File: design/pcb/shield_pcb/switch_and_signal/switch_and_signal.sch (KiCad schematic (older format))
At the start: 8 parts

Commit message: May include some of the refactoring of the schematic into Arduino shield template. Updated library references b/c 2337b83b kicad build wanted it. Broke some things and will need to fix.
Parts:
- Q?: symbol IRL620 -> choice_shield:IRL620
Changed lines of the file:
@@
-EESchema Schematic File Version 3
-LIBS:choice_shield
-LIBS:power
-LIBS:device
-LIBS:linear
-LIBS:regul
-LIBS:adc-dac
-LIBS:memory
-LIBS:xilinx
-LIBS:microcontrollers
-LIBS:dsp
-LIBS:microchip
-LIBS:analog_switches
-LIBS:motorola
-LIBS:texas
-LIBS:intel
-LIBS:audio
-LIBS:interface
-LIBS:digital-audio
-LIBS:philips
-LIBS:cypress
-LIBS:siliconi
-LIBS:opto
-LIBS:atmel
-LIBS:contrib
-LIBS:Connector
-LIBS:Valve
-LIBS:Diode
-LIBS:Display
-LIBS:Transistor
-LIBS:Logic_CMOS_4000
-LIBS:Logic_74xx
+EESchema Schematic File Version 4
 LIBS:shield_pcb-cache
 EELAYER 26 0
@@
 $Descr A4 11693 8268
 encoding utf-8
-Sheet 1 1
+Sheet 10 18
 Title ""
 Date ""
@@
 AR Path="/5A04F7C4/5A020264" Ref="R?"  Part="1"
 AR Path="/5A04FF59/5A020264" Ref="R?"  Part="1"
+AR Path="/5A053B90/5A020264" Ref="R?"  Part="1"
 F 0 "R?" V 2350 2750 50  0000 L CNN
 F 1 "150" V 2450 2750 50  0000 L CNN
@@
 AR Path="/5A04F7C4/5A0202C8" Ref="R?"  Part="1"
 AR Path="/5A04FF59/5A0202C8" Ref="R?"  Part="1"
+AR Path="/5A053B90/5A0202C8" Ref="R?"  Part="1"
 F 0 "R?" H 3120 3246 50  0000 L CNN
 F 1 "100K" H 3120 3155 50  0000 L CNN
@@
 AR Path="/5A04F7C4/5A020329" Ref="R?"  Part="1"
 AR Path="/5A04FF59/5A020329" Ref="R?"  Part="1"
+AR Path="/5A053B90/5A020329" Ref="R?"  Part="1"
 F 0 "R?" H 3720 1996 50  0000 L CNN
 F 1 "150K" H 3720 1905 50  0000 L CNN
@@
 AR Path="/5A04F7C4/5A020365" Ref="R?"  Part="1"
 AR Path="/5A04FF59/5A020365" Ref="R?"  Part="1"
+AR Path="/5A053B90/5A020365" Ref="R?"  Part="1"
 F 0 "R?" V 3950 1500 50  0000 L CNN
 F 1 "160K,0.25W" V 4050 1500 50  0000 L CNN
@@
 AR Path="/5A04F7C4/5A0203AA" Ref="R?"  Part="1"
 AR Path="/5A04FF59/5A0203AA" Ref="R?"  Part="1"
+AR Path="/5A053B90/5A0203AA" Ref="R?"  Part="1"
 F 0 "R?" V 3950 2150 50  0000 L CNN
 F 1 "160K,0.25W" V 4050 2150 50  0000 L CNN
@@
 AR Path="/5A04F7C4/5A020460" Ref="D?"  Part="1"
 AR Path="/5A04FF59/5A020460" Ref="D?"  Part="1"
+AR Path="/5A053B90/5A020460" Ref="D?"  Part="1"
 F 0 "D?" V 4600 1600 50  0000 C CNN
 F 1 "D" V 4700 1550 50  0000 C CNN
@@
 AR Path="/5A04F7C4/5A020509" Ref="D?"  Part="1"
 AR Path="/5A04FF59/5A020509" Ref="D?"  Part="1"
+AR Path="/5A053B90/5A020509" Ref="D?"  Part="1"
 F 0 "D?" V 4600 2250 50  0000 C CNN
 F 1 "D" V 4700 2200 50  0000 C CNN
@@
 $EndComp
 $Comp
-L IRL620 Q?
+L choice_shield:IRL620 Q?
 U 1 1 5A04EA8A
 P 3550 2850
 AR Path="/5A04F7C4/5A04EA8A" Ref="Q?"  Part="1"
 AR Path="/5A04FF59/5A04EA8A" Ref="Q?"  Part="1"
+AR Path="/5A053B90/5A04EA8A" Ref="Q?"  Part="1"
 F 0 "Q?" H 3756 2896 50  0000 L CNN
 F 1 "IRL620" H 3756 2805 50  0000 L CNN
@@
 AR Path="/5A04F7C4/5A04F122" Ref="#PWR?"  Part="1"
 AR Path="/5A04FF59/5A04F122" Ref="#PWR?"  Part="1"
+AR Path="/5A053B90/5A04F122" Ref="#PWR?"  Part="1"
 F 0 "#PWR?" H 3350 3400 50  0001 C CNN
 F 1 "GND" H 3355 3477 50  0000 C CNN
@@
 AR Path="/5A04F7C4/5A04FCD5" Ref="#PWR?"  Part="1"
 AR Path="/5A04FF59/5A04FCD5" Ref="#PWR?"  Part="1"
+AR Path="/5A053B90/5A04FCD5" Ref="#PWR?"  Part="1"
 F 0 "#PWR?" H 4650 1750 50  0001 C CNN
 F 1 "VCC" H 4667 2073 50  0000 C CNN
@@
 AR Path="/5A04F7C4/5A04FD15" Ref="#PWR?"  Part="1"
 AR Path="/5A04FF59/5A04FD15" Ref="#PWR?"  Part="1"
+AR Path="/5A053B90/5A04FD15" Ref="#PWR?"  Part="1"
 F 0 "#PWR?" H 4650 1100 50  0001 C CNN
 F 1 "VCC" H 4667 1423 50  0000 C CNN

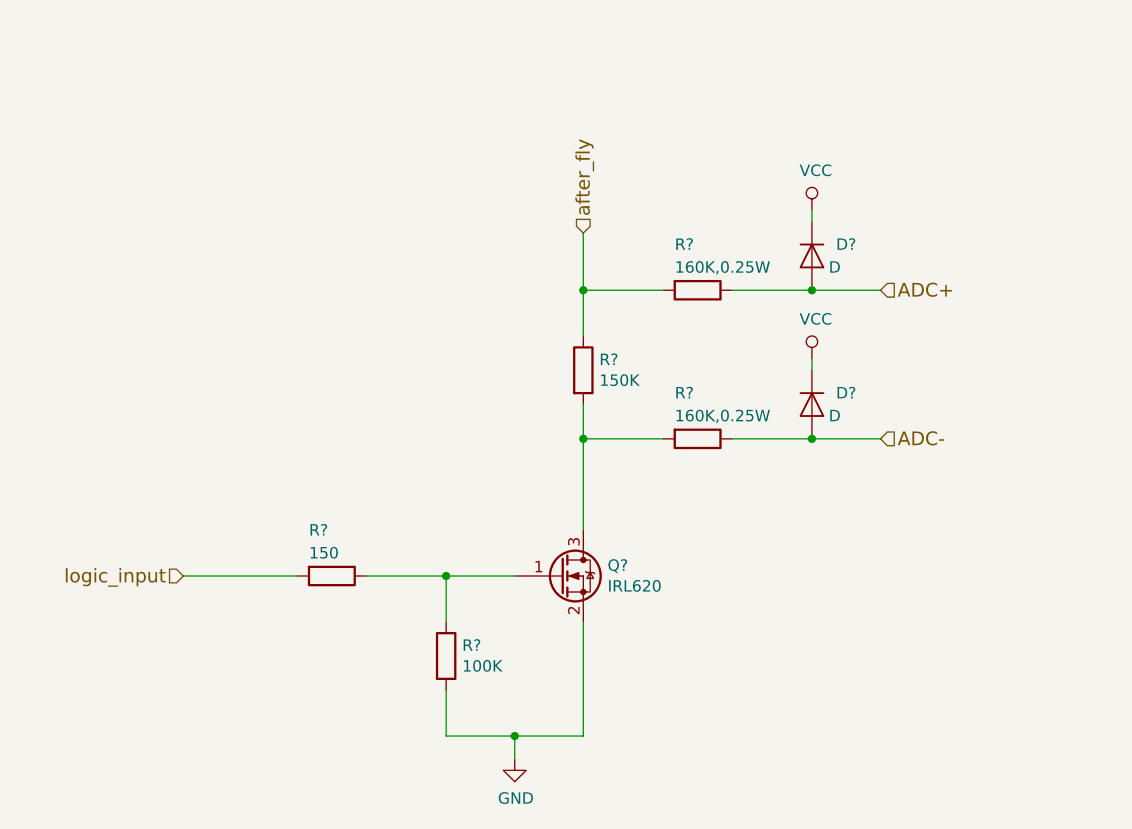
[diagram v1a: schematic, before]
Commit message: Fixed shield schematic, at least for KiCad <= d8f4e35. Added notes to single measurement unit. Updated IRL620 library part to include correct datasheet, etc.
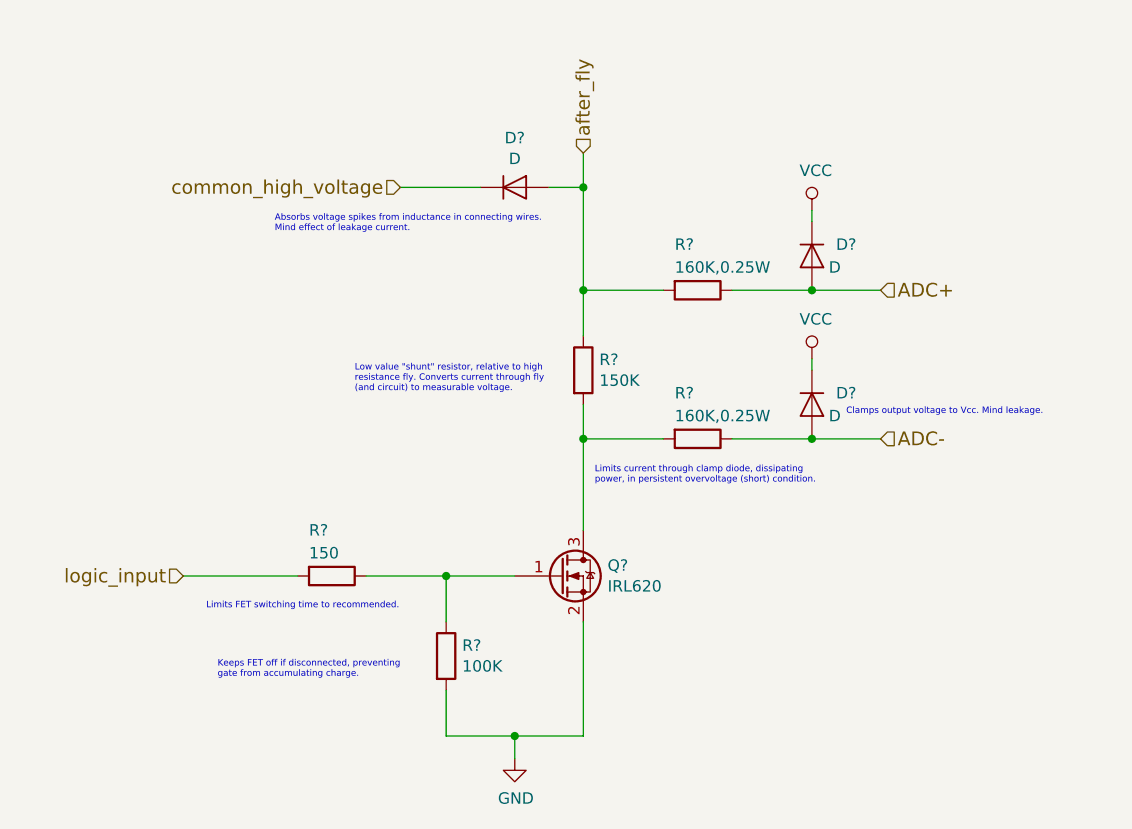
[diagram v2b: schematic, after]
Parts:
- removed Q?: IRL620, TO_SOT_Packages_THT:TO-220-3_Vertical, symbol choice_shield:IRL620
- added D?: D, symbol D
- added Q?: IRL620, TO_SOT_Packages_THT:TO-220-3_Vertical, symbol IRL620
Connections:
- net GND: now also Q?.2 (S)
- net after_fly: now also D?.2 (A)
- net at R?.1, R?.1: now also Q?.1 (G)
- net at R?.2, R?.2: now also Q?.3 (D)
- new net common_high_voltage: D?.1 (K)
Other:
- note added: "Absorbs voltage spikes from inductance in connecting wires.\nMind effect of leakage current."
- note added: "Clamps output voltage to Vcc. Mind leakage."
- note added: "Keeps FET off if disconnected, preventing \ngate from accumulating charge."
- note added: "Limits FET switching time to recommended."
- note added: "Limits current through clamp diode, dissipating \npower, in persistent overvoltage (short) condition."
- note added: "Low value "shunt" resistor, relative to high \nresistance fly. Converts current through fly \n(and circuit) to measurable voltage."
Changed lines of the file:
@@
-EESchema Schematic File Version 4
+EESchema Schematic File Version 3
+LIBS:choice_shield
+LIBS:device
+LIBS:Connector
+LIBS:Transistor
+LIBS:analog_devices
+LIBS:analog_switches
+LIBS:atmel
+LIBS:power
 LIBS:shield_pcb-cache
 EELAYER 26 0
@@
 AR Path="/5A04FF59/5A020264" Ref="R?"  Part="1"
 AR Path="/5A053B90/5A020264" Ref="R?"  Part="1"
+AR Path="/5A050A02/5A020264" Ref="R?"  Part="1"
 F 0 "R?" V 2350 2750 50  0000 L CNN
 F 1 "150" V 2450 2750 50  0000 L CNN
@@
 AR Path="/5A04FF59/5A0202C8" Ref="R?"  Part="1"
 AR Path="/5A053B90/5A0202C8" Ref="R?"  Part="1"
+AR Path="/5A050A02/5A0202C8" Ref="R?"  Part="1"
 F 0 "R?" H 3120 3246 50  0000 L CNN
 F 1 "100K" H 3120 3155 50  0000 L CNN
@@
 AR Path="/5A04FF59/5A020329" Ref="R?"  Part="1"
 AR Path="/5A053B90/5A020329" Ref="R?"  Part="1"
+AR Path="/5A050A02/5A020329" Ref="R?"  Part="1"
 F 0 "R?" H 3720 1996 50  0000 L CNN
 F 1 "150K" H 3720 1905 50  0000 L CNN
@@
 AR Path="/5A04FF59/5A020365" Ref="R?"  Part="1"
 AR Path="/5A053B90/5A020365" Ref="R?"  Part="1"
+AR Path="/5A050A02/5A020365" Ref="R?"  Part="1"
 F 0 "R?" V 3950 1500 50  0000 L CNN
 F 1 "160K,0.25W" V 4050 1500 50  0000 L CNN
@@
 AR Path="/5A04FF59/5A0203AA" Ref="R?"  Part="1"
 AR Path="/5A053B90/5A0203AA" Ref="R?"  Part="1"
+AR Path="/5A050A02/5A0203AA" Ref="R?"  Part="1"
 F 0 "R?" V 3950 2150 50  0000 L CNN
 F 1 "160K,0.25W" V 4050 2150 50  0000 L CNN
@@
 AR Path="/5A04FF59/5A020460" Ref="D?"  Part="1"
 AR Path="/5A053B90/5A020460" Ref="D?"  Part="1"
+AR Path="/5A050A02/5A020460" Ref="D?"  Part="1"
 F 0 "D?" V 4600 1600 50  0000 C CNN
 F 1 "D" V 4700 1550 50  0000 C CNN
@@
 AR Path="/5A04FF59/5A020509" Ref="D?"  Part="1"
 AR Path="/5A053B90/5A020509" Ref="D?"  Part="1"
+AR Path="/5A050A02/5A020509" Ref="D?"  Part="1"
 F 0 "D?" V 4600 2250 50  0000 C CNN
 F 1 "D" V 4700 2200 50  0000 C CNN
@@
 	1    4650 2100
 	0    1    1    0
-$EndComp
-$Comp
-L choice_shield:IRL620 Q?
-U 1 1 5A04EA8A
-P 3550 2850
-AR Path="/5A04F7C4/5A04EA8A" Ref="Q?"  Part="1"
-AR Path="/5A04FF59/5A04EA8A" Ref="Q?"  Part="1"
-AR Path="/5A053B90/5A04EA8A" Ref="Q?"  Part="1"
-F 0 "Q?" H 3756 2896 50  0000 L CNN
-F 1 "IRL620" H 3756 2805 50  0000 L CNN
-F 2 "TO_SOT_Packages_THT:TO-220-3_Vertical" H 3750 2775 50  0001 L CIN
-F 3 "https://www.fairchildsemi.com/datasheets/BS/BSS138.pdf" H 3550 2850 50  0001 L CNN
-	1    3550 2850
-	1    0    0    -1
 $EndComp
 $Comp
@@
 AR Path="/5A04FF59/5A04F122" Ref="#PWR?"  Part="1"
 AR Path="/5A053B90/5A04F122" Ref="#PWR?"  Part="1"
+AR Path="/5A050A02/5A04F122" Ref="#PWR?"  Part="1"
 F 0 "#PWR?" H 3350 3400 50  0001 C CNN
 F 1 "GND" H 3355 3477 50  0000 C CNN
@@
 F 3 "" H 3350 3650 50  0001 C CNN
 	1    3350 3650
-	1    0    0    -1
-$EndComp
-$Comp
-L VCC #PWR?
-U 1 1 5A04FCD5
-P 4650 1900
-AR Path="/5A04F7C4/5A04FCD5" Ref="#PWR?"  Part="1"
-AR Path="/5A04FF59/5A04FCD5" Ref="#PWR?"  Part="1"
-AR Path="/5A053B90/5A04FCD5" Ref="#PWR?"  Part="1"
-F 0 "#PWR?" H 4650 1750 50  0001 C CNN
-F 1 "VCC" H 4667 2073 50  0000 C CNN
-F 2 "" H 4650 1900 50  0001 C CNN
-F 3 "" H 4650 1900 50  0001 C CNN
-	1    4650 1900
 	1    0    0    -1
 $EndComp
@@
 AR Path="/5A04FF59/5A04FD15" Ref="#PWR?"  Part="1"
 AR Path="/5A053B90/5A04FD15" Ref="#PWR?"  Part="1"
+AR Path="/5A050A02/5A04FD15" Ref="#PWR?"  Part="1"
 F 0 "#PWR?" H 4650 1100 50  0001 C CNN
 F 1 "VCC" H 4667 1423 50  0000 C CNN
@@
 	4000 1600 3650 1600
 Wire Wire Line
-	3650 1350 3650 1800
+	3650 1000 3650 1800
 Wire Wire Line
 	4300 1600 4950 1600
@@
 Wire Wire Line
 	1900 2850 2400 2850
-Text HLabel 3650 1350 1    60   Input ~ 0
+Text HLabel 3650 1000 1    60   Input ~ 0
 after_fly
 Connection ~ 3650 1600
@@
 	4000 2250 3650 2250
 Connection ~ 3650 2250
+$Comp
+L VCC #PWR?
+U 1 1 5A04FCD5
+P 4650 1900
+AR Path="/5A04F7C4/5A04FCD5" Ref="#PWR?"  Part="1"
+AR Path="/5A04FF59/5A04FCD5" Ref="#PWR?"  Part="1"
+AR Path="/5A053B90/5A04FCD5" Ref="#PWR?"  Part="1"
+AR Path="/5A050A02/5A04FCD5" Ref="#PWR?"  Part="1"
+F 0 "#PWR?" H 4650 1750 50  0001 C CNN
+F 1 "VCC" H 4667 2073 50  0000 C CNN
+F 2 "" H 4650 1900 50  0001 C CNN
+F 3 "" H 4650 1900 50  0001 C CNN
+	1    4650 1900
+	1    0    0    -1
+$EndComp
+$Comp
+L IRL620 Q?
+U 1 1 5A0A1124
+P 3550 2850
+F 0 "Q?" H 3756 2896 50  0000 L CNN
+F 1 "IRL620" H 3756 2805 50  0000 L CNN
+F 2 "TO_SOT_Packages_THT:TO-220-3_Vertical" H 3750 2775 50  0001 L CIN
+F 3 "https://www.vishay.com/docs/91301/91301.pdf" H 3550 2850 50  0001 L CNN
+	1    3550 2850
+	1    0    0    -1
+$EndComp
+$Comp
+L D D?
+U 1 1 5A0A33AC
+P 3350 1150
+F 0 "D?" H 3350 1366 50  0000 C CNN
+F 1 "D" H 3350 1275 50  0000 C CNN
+F 2 "" H 3350 1150 50  0001 C CNN
+F 3 "" H 3350 1150 50  0001 C CNN
+	1    3350 1150
+	1    0    0    -1
+$EndComp
+Text HLabel 2850 1150 0    60   Input ~ 0
+common_high_voltage
+Wire Wire Line
+	2850 1150 3200 1150
+Wire Wire Line
+	3500 1150 3650 1150
+Connection ~ 3650 1150
+Text Notes 2300 1350 0    28   ~ 0
+Absorbs voltage spikes from inductance in connecting wires.\nMind effect of leakage current.
+Text Notes 2050 3300 0    28   ~ 0
+Keeps FET off if disconnected, preventing \ngate from accumulating charge.
+Text Notes 2000 3000 0    28   ~ 0
+Limits FET switching time to recommended.
+Text Notes 3700 2450 0    28   ~ 0
+Limits current through clamp diode, dissipating \npower, in persistent overvoltage (short) condition.
+Text Notes 4800 2150 0    28   ~ 0
+Clamps output voltage to Vcc. Mind leakage.
+Text Notes 2650 2050 0    28   ~ 0
+Low value "shunt" resistor, relative to high \nresistance fly. Converts current through fly \n(and circuit) to measurable voltage.
 $EndSCHEMATC

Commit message: Working on shift registers and optical isolators. Don't think I'll try to find some elegant solution to use chips to cycle through shocked channels. May keep measurement SR separate. Added most datasheets. Will layout PCB soon.
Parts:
- removed D? (x2): D, symbol D
- removed R? (x2): 160K,0.25W, symbol R
- added D?: MMSZ5231B, 500mW, 5.1V, 5uA max reverse leakage, symbol D_Zener
- added D? (x4): D, symbol D
- added J? (x3): GS2, Connectors:GS2, symbol GS2
- added R?: 39K, 5%, 1W, symbol R
- added R? (x2): 160K, 1/4W, symbol R
- R?: value 150K -> 15K
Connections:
- net labels added: +5VA, GNDA
- net labels removed: GND, VCC
- wire segments 17 -> 52
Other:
- note added: "Absorbs (-) voltage spikes from inductance in connecting \nwires. Mind effect of leakage current."
- note added: "All diodes and resistors to the right of the shunt\nresistor should be dispensable, if the resistor and\nzener above the shunt works well enough."
- note added: "TODO any way to indicate that these jumpers are NC?"
- note removed: "Absorbs voltage spikes from inductance in connecting wires.\nMind effect of leakage current."
- note removed: "Clamps output voltage to Vcc. Mind leakage."
- note removed: "Limits current through clamp diode, dissipating \npower, in persistent overvoltage (short) condition."
- moved on the sheet: D?, Q?, R?

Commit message: Mostly done with digital input isolation subsheets. Planning to refactor switch_and_signal.sch to this directly, as other subsheets. May break.
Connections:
- wire segments 52 -> 35
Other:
- note added: "TODO is 100K an appropriate pulldown here?\nwhy or why not? maybe doesn't matter?\n(just seems larger than recommendation for \nlogic ICs, but this FET may be a different beast)"
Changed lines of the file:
@@
 $Descr A4 11693 8268
 encoding utf-8
-Sheet 10 18
+Sheet 10 24
 Title ""
 Date ""
@@
 U 1 1 5A0F7C0B
 P 4700 2550
+AR Path="/5A053B90/5A0F7C0B" Ref="D?"  Part="1"
+AR Path="/5A053B9C/5A0F7C0B" Ref="D?"  Part="1"
 F 0 "D?" H 4700 2766 50  0000 C CNN
 F 1 "MMSZ5231B, 500mW, 5.1V, 5uA max reverse leakage" H 5650 2700 50  0000 C CNN
@@
 U 1 1 5A0F7E6B
 P 4300 2100
+AR Path="/5A053B90/5A0F7E6B" Ref="R?"  Part="1"
+AR Path="/5A053B9C/5A0F7E6B" Ref="R?"  Part="1"
 F 0 "R?" H 4370 2146 50  0000 L CNN
 F 1 "39K, 5%, 1W" H 4370 2055 50  0000 L CNN
@@
 U 1 1 5A0F912E
 P 5600 3150
+AR Path="/5A053B90/5A0F912E" Ref="R?"  Part="1"
+AR Path="/5A053B9C/5A0F912E" Ref="R?"  Part="1"
 F 0 "R?" V 5393 3150 50  0000 C CNN
 F 1 "160K, 1/4W" V 5484 3150 50  0000 C CNN
@@
 U 1 1 5A0F91CC
 P 5600 4150
+AR Path="/5A053B90/5A0F91CC" Ref="R?"  Part="1"
+AR Path="/5A053B9C/5A0F91CC" Ref="R?"  Part="1"
 F 0 "R?" V 5393 4150 50  0000 C CNN
 F 1 "160K, 1/4W" V 5484 4150 50  0000 C CNN
@@
 U 1 1 5A0F938E
 P 6000 3000
+AR Path="/5A053B90/5A0F938E" Ref="D?"  Part="1"
+AR Path="/5A053B9C/5A0F938E" Ref="D?"  Part="1"
 F 0 "D?" V 5954 3079 50  0000 L CNN
 F 1 "D" V 6045 3079 50  0000 L CNN
@@
 U 1 1 5A0F9417
 P 6000 4000
+AR Path="/5A053B90/5A0F9417" Ref="D?"  Part="1"
+AR Path="/5A053B9C/5A0F9417" Ref="D?"  Part="1"
 F 0 "D?" V 5954 4079 50  0000 L CNN
 F 1 "D" V 6045 4079 50  0000 L CNN
@@
 $EndComp
 Wire Wire Line
-	3350 4600 3700 4600
-Wire Wire Line
-	3700 4600 4000 4600
+	3350 4600 4000 4600
 Wire Wire Line
 	3700 4800 3700 4600
@@
 	3700 5100 3700 5300
 Wire Wire Line
-	3700 5300 4000 5300
-Wire Wire Line
-	4000 5300 4300 5300
+	3700 5300 4300 5300
 Wire Wire Line
 	4300 5300 4300 4800
@@
 	4850 2550 5100 2550
 Wire Wire Line
-	4300 1300 4300 1450
-Wire Wire Line
-	4300 1450 4300 1850
-Wire Wire Line
-	4300 1850 4300 1950
+	4300 1300 4300 1950
 Connection ~ 4300 1850
 Connection ~ 4300 2300
@@
 	3400 1850 4300 1850
 Wire Wire Line
-	4300 2300 3400 2300
-Wire Wire Line
-	3400 2300 3400 2300
-Wire Wire Line
-	4300 3850 4300 4150
-Wire Wire Line
-	4300 4150 4300 4400
-Wire Wire Line
-	4300 2250 4300 2300
-Wire Wire Line
-	4300 2300 4300 2550
-Wire Wire Line
-	4300 2550 4300 3150
-Wire Wire Line
-	4300 3150 4300 3550
-Wire Wire Line
-	4300 3150 5150 3150
-Wire Wire Line
-	5150 3150 5450 3150
+	3400 2300 4300 2300
+Wire Wire Line
+	4300 3850 4300 4400
+Wire Wire Line
+	4300 2250 4300 3550
+Wire Wire Line
+	4300 3150 5450 3150
 Connection ~ 4300 3150
 Wire Wire Line
@@
 Connection ~ 5150 3150
 Wire Wire Line
-	5750 3150 6000 3150
-Wire Wire Line
-	6000 3150 6750 3150
-Wire Wire Line
-	6750 3150 7450 3150
+	5750 3150 7450 3150
 Wire Wire Line
 	6000 2850 6000 2750
@@
 	6000 3450 6000 3150
 Wire Wire Line
-	4300 4150 5150 4150
-Wire Wire Line
-	5150 4150 5450 4150
+	4300 4150 5450 4150
 Connection ~ 4300 4150
 Wire Wire Line
@@
 Connection ~ 5150 4150
 Wire Wire Line
-	5750 4150 6000 4150
-Wire Wire Line
-	6000 4150 6750 4150
-Wire Wire Line
-	6750 4150 7450 4150
+	5750 4150 7450 4150
 Wire Wire Line
 	6000 3850 6000 3750
@@
 U 1 1 5A116490
 P 6600 3650
+AR Path="/5A053B90/5A116490" Ref="D?"  Part="1"
+AR Path="/5A053B9C/5A116490" Ref="D?"  Part="1"
 F 0 "D?" V 6554 3729 50  0000 L CNN
 F 1 "D" V 6645 3729 50  0000 L CNN
@@
 U 1 1 5A1165C0
 P 6950 3650
+AR Path="/5A053B90/5A1165C0" Ref="D?"  Part="1"
+AR Path="/5A053B9C/5A1165C0" Ref="D?"  Part="1"
 F 0 "D?" V 6996 3571 50  0000 R CNN
 F 1 "D" V 6905 3571 50  0000 R CNN
@@
 $EndComp
 Wire Wire Line
-	6600 3500 6750 3500
-Wire Wire Line
-	6750 3500 6950 3500
+	6600 3500 6950 3500
 Wire Wire Line
 	6750 3500 6750 3150
@@
 Connection ~ 6750 3500
 Wire Wire Line
-	6600 3800 6750 3800
-Wire Wire Line
-	6750 3800 6950 3800
+	6600 3800 6950 3800
 Wire Wire Line
 	6750 3800 6750 4150
@@
 U 1 1 5A1FF590
 P 5600 4450
+AR Path="/5A053B90/5A1FF590" Ref="J?"  Part="1"
+AR Path="/5A053B9C/5A1FF590" Ref="J?"  Part="1"
 F 0 "J?" V 5395 4450 50  0000 C CNN
 F 1 "GS2" V 5486 4450 50  0000 C CNN
@@
 U 1 1 5A1FF735
 P 5600 3450
+AR Path="/5A053B90/5A1FF735" Ref="J?"  Part="1"
+AR Path="/5A053B9C/5A1FF735" Ref="J?"  Part="1"
 F 0 "J?" V 5395 3450 50  0000 C CNN
 F 1 "GS2" V 5486 3450 50  0000 C CNN
@@
 U 1 1 5A1FF948
 P 3400 2100
+AR Path="/5A053B90/5A1FF948" Ref="J?"  Part="1"
+AR Path="/5A053B9C/5A1FF948" Ref="J?"  Part="1"
 F 0 "J?" H 3332 2054 50  0000 R CNN
 F 1 "GS2" H 3332 2145 50  0000 R CNN
@@
 U 1 1 5A1FFEF2
 P 4000 5400
+AR Path="/5A053B90/5A1FFEF2" Ref="#PWR?"  Part="1"
+AR Path="/5A053B9C/5A1FFEF2" Ref="#PWR?"  Part="1"
 F 0 "#PWR?" H 4000 5150 50  0001 C CNN
 F 1 "GNDA" H 4005 5227 50  0000 C CNN
@@
 U 1 1 5A20015F
 P 5100 2550
+AR Path="/5A053B90/5A20015F" Ref="#PWR?"  Part="1"
+AR Path="/5A053B9C/5A20015F" Ref="#PWR?"  Part="1"
 F 0 "#PWR?" H 5100 2300 50  0001 C CNN
 F 1 "GNDA" V 5105 2422 50  0000 R CNN
@@
 U 1 1 5A200249
 P 6000 2750
+AR Path="/5A053B90/5A200249" Ref="#PWR?"  Part="1"
+AR Path="/5A053B9C/5A200249" Ref="#PWR?"  Part="1"
 F 0 "#PWR?" H 6000 2600 50  0001 C CNN
 F 1 "+5VA" H 6015 2923 50  0000 C CNN
@@
 U 1 1 5A20062C
 P 6000 3750
+AR Path="/5A053B90/5A20062C" Ref="#PWR?"  Part="1"
+AR Path="/5A053B9C/5A20062C" Ref="#PWR?"  Part="1"
 F 0 "#PWR?" H 6000 3600 50  0001 C CNN
 F 1 "+5VA" H 6015 3923 50  0000 C CNN
@@
 	1    0    0    -1
 $EndComp
+Text Notes 3000 6150 0    60   ~ 0
+TODO is 100K an appropriate pulldown here?\nwhy or why not? maybe doesn't matter?\n(just seems larger than recommendation for \nlogic ICs, but this FET may be a different beast)
 $EndSCHEMATC
